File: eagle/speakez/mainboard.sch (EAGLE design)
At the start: 29 parts, among them U1 +12v

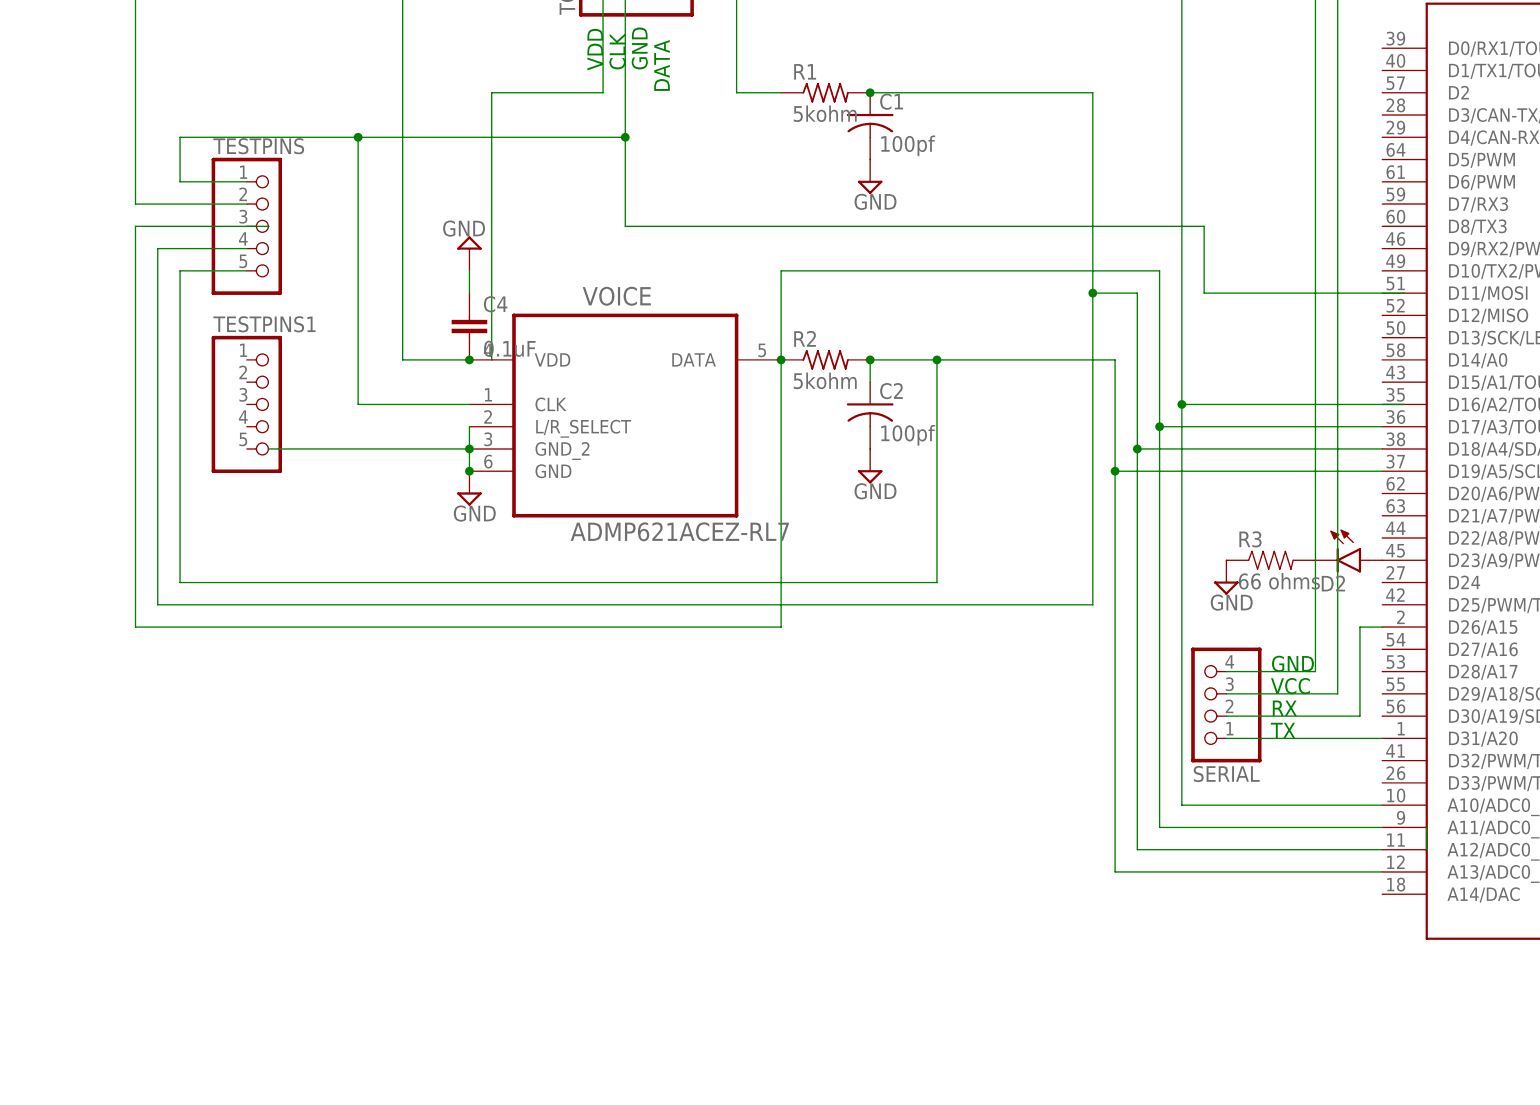
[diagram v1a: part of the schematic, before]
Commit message: added DAC cap + resistor
didn't choose cap value yet. Sent output to a header test pin
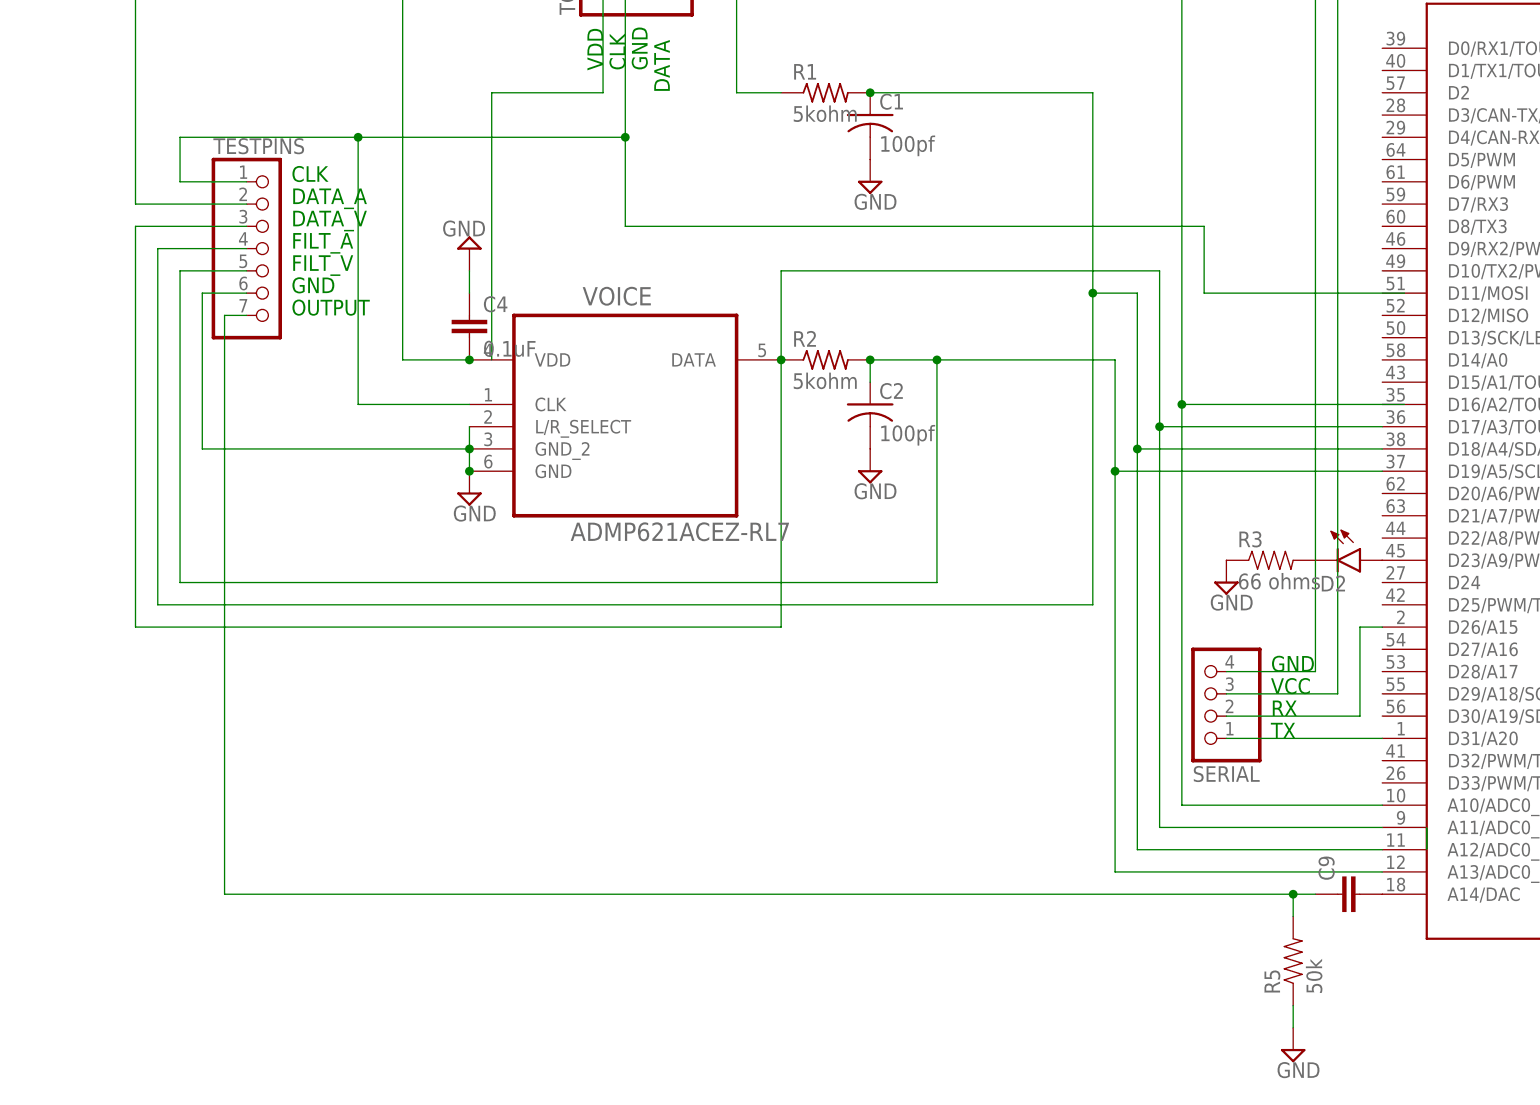
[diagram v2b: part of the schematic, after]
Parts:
- removed TESTPINS1: (no value), pinhead:PINHD-1X5M
- added C9: (no value), SparkFun-Capacitors:CAP0805
- added R5: 50k, SparkFun-Passives:RESISTOR0805-RES
- TESTPINS: device pinhead:PINHD-1X5M -> pinhead:PINHD-1X7
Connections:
- new net N$27: C9.2, U$1.A14/DAC
- new net N$28: C9.1, R5.2, TESTPINS.7
- net GND: now also R5.1, TESTPINS.6
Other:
- note added: "DATA_A"
- note added: "DATA_V"
- note added: "FILT_A"
- note added: "FILT_V"
- note added: "OUTPUT"
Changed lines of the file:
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@@
 <part name="AMBIENT" library="InvenSense-INMP621ACEZ-R7" deviceset="ADMP621ACEZ-RL7" device=""/>
 <part name="VOICE" library="InvenSense-INMP621ACEZ-R7" deviceset="ADMP621ACEZ-RL7" device=""/>
-<part name="TESTPINS" library="pinhead" deviceset="PINHD-1X5" device="M"/>
+<part name="TESTPINS" library="pinhead" deviceset="PINHD-1X7" device=""/>
 <part name="SUPPLY8" library="supply2" deviceset="GND" device=""/>
 <part name="SUPPLY10" library="supply2" deviceset="GND" device=""/>
@@
 <part name="D1" library="SparkFun-DiscreteSemi" deviceset="DIODE" device="SOD123" value="1N5819HW-7-F"/>
 <part name="C3" library="SparkFun-Capacitors" deviceset="CAP" device="0805" value="0.1uF"/>
-<part name="TESTPINS1" library="pinhead" deviceset="PINHD-1X5" device="M"/>
 <part name="SUPPLY4" library="supply2" deviceset="GND" device=""/>
 <part name="U$1" library="Teensy_DIY_v1.0" deviceset="MK20DX256VLH7" device=""/>
@@
 <part name="PROGRAMMER" library="pel_hdr" deviceset="PH1X5" device="-05"/>
 <part name="SERIAL" library="pinhead" deviceset="PINHD-1X4" device=""/>
+<part name="R5" library="SparkFun-Passives" deviceset="RESISTOR" device="0805-RES" value="50k"/>
+<part name="C9" library="SparkFun-Capacitors" deviceset="CAP" device="0805"/>
+<part name="SUPPLY5" library="supply2" deviceset="GND" device=""/>
 </parts>
 <sheets>
@@
 <text x="104.14" y="-12.7" size="1.778" layer="91">TX</text>
 <text x="104.14" y="-10.16" size="1.778" layer="91">RX</text>
+<text x="-7.62" y="50.8" size="1.778" layer="91">CLK</text>
+<text x="-7.62" y="48.26" size="1.778" layer="91">DATA_A</text>
+<text x="-7.62" y="45.72" size="1.778" layer="91">DATA_V</text>
+<text x="-7.62" y="43.18" size="1.778" layer="91">FILT_A</text>
+<text x="-7.62" y="40.64" size="1.778" layer="91">FILT_V</text>
+<text x="-7.62" y="38.1" size="1.778" layer="91">GND</text>
+<text x="-7.62" y="35.56" size="1.778" layer="91">OUTPUT</text>
 </plain>
 <instances>
@@
 <instance part="AMBIENT" gate="A" x="-68.58" y="45.72"/>
 <instance part="VOICE" gate="A" x="30.48" y="27.94"/>
-<instance part="TESTPINS" gate="A" x="-10.16" y="45.72"/>
+<instance part="TESTPINS" gate="A" x="-10.16" y="43.18"/>
 <instance part="SUPPLY8" gate="GND" x="12.7" y="15.24"/>
 <instance part="SUPPLY10" gate="GND" x="12.7" y="43.18" rot="R180"/>
@@
 <instance part="D1" gate="G$1" x="121.92" y="104.14" rot="R270"/>
 <instance part="C3" gate="G$1" x="-93.98" y="43.18"/>
-<instance part="TESTPINS1" gate="A" x="-10.16" y="25.4"/>
 <instance part="SUPPLY4" gate="GND" x="33.02" y="88.9" rot="R180"/>
 <instance part="U$1" gate="G$1" x="144.78" y="15.24"/>
@@
 <instance part="PROGRAMMER" gate="G$1" x="198.12" y="-7.62" rot="R180"/>
 <instance part="SERIAL" gate="A" x="96.52" y="-7.62" rot="R180"/>
+<instance part="R5" gate="G$1" x="106.68" y="-38.1" rot="R90"/>
+<instance part="C9" gate="G$1" x="114.3" y="-30.48" rot="R90"/>
+<instance part="SUPPLY5" gate="GND" x="106.68" y="-48.26"/>
 </instances>
 <busses>
@@
 <wire x1="83.82" y1="2.54" x2="-22.86" y2="2.54" width="0.1524" layer="91"/>
 <wire x1="-22.86" y1="2.54" x2="-22.86" y2="43.18" width="0.1524" layer="91"/>
-<pinref part="TESTPINS" gate="A" pin="4"/>
-<wire x1="-12.7" y1="43.18" x2="-22.86" y2="43.18" width="0.1524" layer="91"/>
 <wire x1="83.82" y1="38.1" x2="88.9" y2="38.1" width="0.1524" layer="91"/>
 <junction x="83.82" y="38.1"/>
@@
 <pinref part="U$1" gate="G$1" pin="A12/ADC0_DP3"/>
 <wire x1="88.9" y1="-25.4" x2="116.84" y2="-25.4" width="0.1524" layer="91"/>
+<pinref part="TESTPINS" gate="A" pin="4"/>
+<wire x1="-22.86" y1="43.18" x2="-12.7" y2="43.18" width="0.1524" layer="91"/>
 </segment>
 </net>
@@
 <wire x1="-20.32" y1="40.64" x2="-20.32" y2="5.08" width="0.1524" layer="91"/>
 <wire x1="-20.32" y1="5.08" x2="66.04" y2="5.08" width="0.1524" layer="91"/>
-<pinref part="TESTPINS" gate="A" pin="5"/>
-<wire x1="-12.7" y1="40.64" x2="-20.32" y2="40.64" width="0.1524" layer="91"/>
 <wire x1="86.36" y1="17.78" x2="86.36" y2="30.48" width="0.1524" layer="91"/>
 <wire x1="86.36" y1="30.48" x2="66.04" y2="30.48" width="0.1524" layer="91"/>
@@
 <pinref part="U$1" gate="G$1" pin="A13/ADC0_DM3"/>
 <wire x1="86.36" y1="-27.94" x2="116.84" y2="-27.94" width="0.1524" layer="91"/>
+<pinref part="TESTPINS" gate="A" pin="5"/>
+<wire x1="-20.32" y1="40.64" x2="-12.7" y2="40.64" width="0.1524" layer="91"/>
 </segment>
 </net>
@@
 <junction x="12.7" y="20.32"/>
 <junction x="12.7" y="17.78"/>
-<wire x1="-10.16" y1="20.32" x2="12.7" y2="20.32" width="0.1524" layer="91"/>
+<wire x1="-17.78" y1="20.32" x2="12.7" y2="20.32" width="0.1524" layer="91"/>
+<pinref part="TESTPINS" gate="A" pin="6"/>
+<wire x1="-12.7" y1="38.1" x2="-17.78" y2="38.1" width="0.1524" layer="91"/>
+<wire x1="-17.78" y1="38.1" x2="-17.78" y2="20.32" width="0.1524" layer="91"/>
 </segment>
 <segment>
@@
 <pinref part="R3" gate="G$1" pin="1"/>
 <pinref part="SUPPLY3" gate="GND" pin="GND"/>
+</segment>
+<segment>
+<pinref part="R5" gate="G$1" pin="1"/>
+<pinref part="SUPPLY5" gate="GND" pin="GND"/>
+<wire x1="106.68" y1="-43.18" x2="106.68" y2="-45.72" width="0.1524" layer="91"/>
 </segment>
 </net>
@@
 <wire x1="48.26" y1="0" x2="-25.4" y2="0" width="0.1524" layer="91"/>
 <wire x1="-25.4" y1="0" x2="-25.4" y2="45.72" width="0.1524" layer="91"/>
-<pinref part="TESTPINS" gate="A" pin="3"/>
-<wire x1="-25.4" y1="45.72" x2="-12.7" y2="45.72" width="0.1524" layer="91"/>
-<wire x1="-12.7" y1="45.72" x2="-10.16" y2="45.72" width="0.1524" layer="91"/>
 <wire x1="91.44" y1="22.86" x2="91.44" y2="40.64" width="0.1524" layer="91"/>
 <wire x1="91.44" y1="40.64" x2="48.26" y2="40.64" width="0.1524" layer="91"/>
@@
 <pinref part="U$1" gate="G$1" pin="A11/ADC0_DP0"/>
 <wire x1="91.44" y1="-22.86" x2="116.84" y2="-22.86" width="0.1524" layer="91"/>
+<pinref part="TESTPINS" gate="A" pin="3"/>
+<wire x1="-25.4" y1="45.72" x2="-12.7" y2="45.72" width="0.1524" layer="91"/>
 </segment>
 </net>
@@
 <junction x="0" y="55.88"/>
 <wire x1="-20.32" y1="55.88" x2="-20.32" y2="50.8" width="0.1524" layer="91"/>
-<pinref part="TESTPINS" gate="A" pin="1"/>
-<wire x1="-20.32" y1="50.8" x2="-12.7" y2="50.8" width="0.1524" layer="91"/>
 <wire x1="0" y1="55.88" x2="0" y2="25.4" width="0.1524" layer="91"/>
 <pinref part="VOICE" gate="A" pin="CLK"/>
@@
 <wire x1="119.38" y1="38.1" x2="96.52" y2="38.1" width="0.1524" layer="91"/>
 <wire x1="96.52" y1="38.1" x2="96.52" y2="45.72" width="0.1524" layer="91"/>
+<pinref part="TESTPINS" gate="A" pin="1"/>
+<wire x1="-20.32" y1="50.8" x2="-12.7" y2="50.8" width="0.1524" layer="91"/>
 </segment>
 </net>
@@
 <pinref part="TOAMBIENT" gate="A" pin="4"/>
 <wire x1="35.56" y1="73.66" x2="43.18" y2="73.66" width="0.1524" layer="91"/>
-<pinref part="TESTPINS" gate="A" pin="2"/>
 <pinref part="R1" gate="G$1" pin="1"/>
 <wire x1="43.18" y1="60.96" x2="48.26" y2="60.96" width="0.1524" layer="91"/>
@@
 <wire x1="43.18" y1="83.82" x2="-25.4" y2="83.82" width="0.1524" layer="91"/>
 <wire x1="-25.4" y1="83.82" x2="-25.4" y2="48.26" width="0.1524" layer="91"/>
-<wire x1="-25.4" y1="48.26" x2="-12.7" y2="48.26" width="0.1524" layer="91"/>
 <junction x="43.18" y="73.66"/>
 <wire x1="43.18" y1="73.66" x2="93.98" y2="73.66" width="0.1524" layer="91"/>
@@
 <pinref part="U$1" gate="G$1" pin="A10/ADC0_DM0"/>
 <wire x1="93.98" y1="-20.32" x2="116.84" y2="-20.32" width="0.1524" layer="91"/>
+<pinref part="TESTPINS" gate="A" pin="2"/>
+<wire x1="-25.4" y1="48.26" x2="-12.7" y2="48.26" width="0.1524" layer="91"/>
 </segment>
 </net>
@@
 </segment>
 </net>
+<net name="N$27" class="0">
+<segment>
+<pinref part="U$1" gate="G$1" pin="A14/DAC"/>
+<pinref part="C9" gate="G$1" pin="2"/>
+</segment>
+</net>
+<net name="N$28" class="0">
+<segment>
+<pinref part="C9" gate="G$1" pin="1"/>
+<wire x1="109.22" y1="-30.48" x2="106.68" y2="-30.48" width="0.1524" layer="91"/>
+<pinref part="R5" gate="G$1" pin="2"/>
+<wire x1="106.68" y1="-30.48" x2="106.68" y2="-33.02" width="0.1524" layer="91"/>
+<wire x1="106.68" y1="-30.48" x2="-15.24" y2="-30.48" width="0.1524" layer="91"/>
+<junction x="106.68" y="-30.48"/>
+<pinref part="TESTPINS" gate="A" pin="7"/>
+<wire x1="-12.7" y1="35.56" x2="-15.24" y2="35.56" width="0.1524" layer="91"/>
+<wire x1="-15.24" y1="35.56" x2="-15.24" y2="-30.48" width="0.1524" layer="91"/>
+</segment>
+</net>

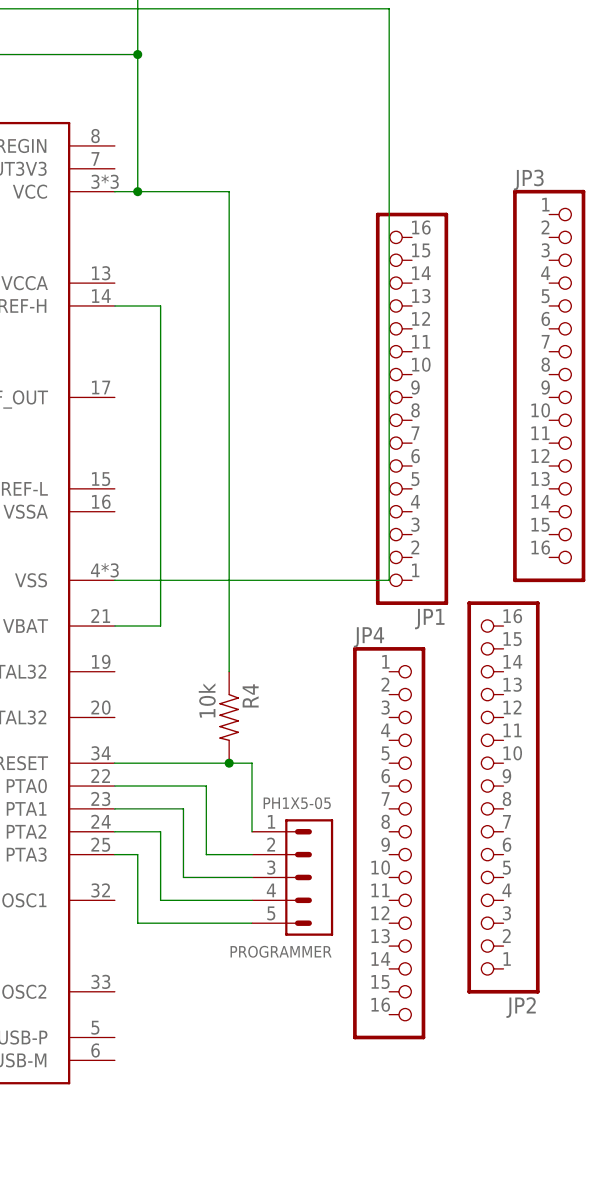
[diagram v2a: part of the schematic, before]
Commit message: test pins for VCC and RESET
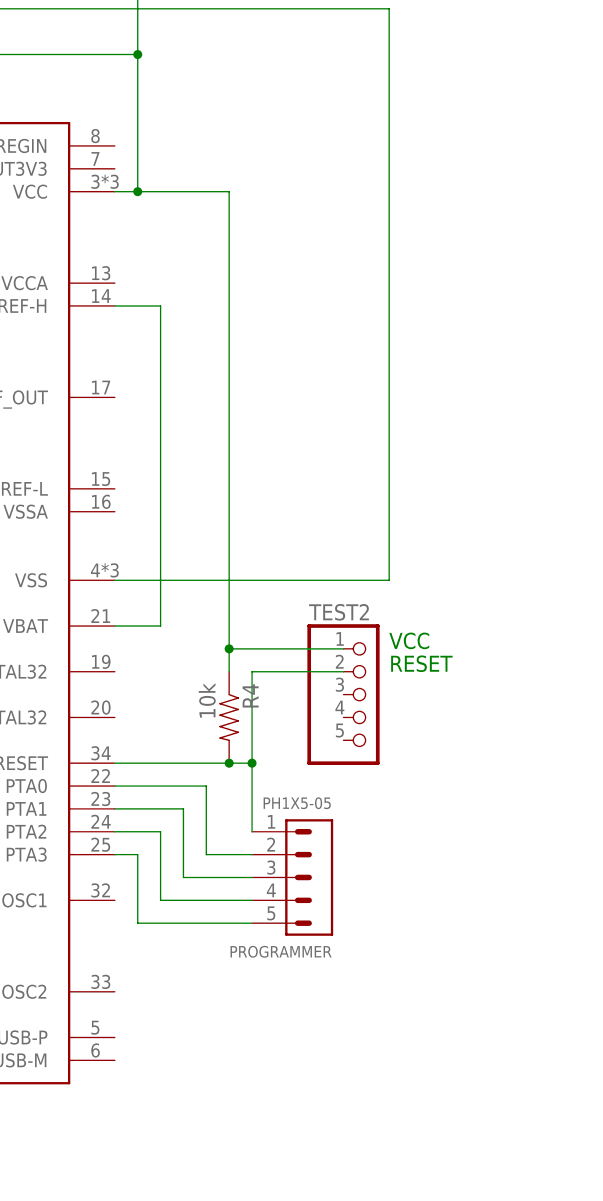
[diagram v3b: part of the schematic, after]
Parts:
- removed JP1, JP2, JP3, JP4: (no value), pinhead:PINHD-1X16
- added TEST2: (no value), pinhead:PINHD-1X5
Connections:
- net N$16: now also TEST2.1
- net N$20: now also TEST2.2
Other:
- note added: "RESET"
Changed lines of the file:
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@@
 <part name="SUPPLY4" library="supply2" deviceset="GND" device=""/>
 <part name="U$1" library="Teensy_DIY_v1.0" deviceset="MK20DX256VLH7" device=""/>
-<part name="JP1" library="pinhead" deviceset="PINHD-1X16" device=""/>
-<part name="JP2" library="pinhead" deviceset="PINHD-1X16" device=""/>
-<part name="JP3" library="pinhead" deviceset="PINHD-1X16" device=""/>
-<part name="JP4" library="pinhead" deviceset="PINHD-1X16" device=""/>
 <part name="U1" library="SparkFun-PowerIC" deviceset="V_REG_78XX" device="7812" value="+12v"/>
 <part name="C5" library="SparkFun-Capacitors" deviceset="CAP" device="0805" value="2.2uF"/>
@@
 <part name="C9" library="SparkFun-Capacitors" deviceset="CAP" device="0805"/>
 <part name="SUPPLY5" library="supply2" deviceset="GND" device=""/>
+<part name="TEST2" library="pinhead" deviceset="PINHD-1X5" device=""/>
 </parts>
 <sheets>
@@
 <text x="-7.62" y="38.1" size="1.778" layer="91">GND</text>
 <text x="-7.62" y="35.56" size="1.778" layer="91">OUTPUT</text>
+<text x="205.74" y="12.7" size="1.778" layer="91">VCC</text>
+<text x="205.74" y="10.16" size="1.778" layer="91">RESET</text>
 </plain>
 <instances>
@@
 <instance part="SUPPLY4" gate="GND" x="33.02" y="88.9" rot="R180"/>
 <instance part="U$1" gate="G$1" x="144.78" y="15.24"/>
-<instance part="JP1" gate="A" x="205.74" y="38.1" rot="R180"/>
-<instance part="JP2" gate="A" x="215.9" y="-5.08" rot="R180"/>
-<instance part="JP3" gate="A" x="226.06" y="43.18"/>
-<instance part="JP4" gate="A" x="208.28" y="-7.62"/>
 <instance part="U1" gate="G$1" x="129.54" y="101.6"/>
 <instance part="C5" gate="G$1" x="121.92" y="86.36"/>
@@
 <instance part="C9" gate="G$1" x="114.3" y="-30.48" rot="R90"/>
 <instance part="SUPPLY5" gate="GND" x="106.68" y="-48.26"/>
+<instance part="TEST2" gate="A" x="203.2" y="7.62"/>
 </instances>
 <busses>
@@
 <junction x="177.8" y="63.5"/>
 <pinref part="R4" gate="G$1" pin="1"/>
-<wire x1="187.96" y1="63.5" x2="187.96" y2="10.16" width="0.1524" layer="91"/>
+<wire x1="187.96" y1="63.5" x2="187.96" y2="12.7" width="0.1524" layer="91"/>
+<wire x1="187.96" y1="12.7" x2="187.96" y2="10.16" width="0.1524" layer="91"/>
 <wire x1="177.8" y1="78.74" x2="111.76" y2="78.74" width="0.1524" layer="91"/>
 <junction x="177.8" y="78.74"/>
@@
 <pinref part="SERIAL" gate="A" pin="3"/>
 <wire x1="111.76" y1="-7.62" x2="99.06" y2="-7.62" width="0.1524" layer="91"/>
+<pinref part="TEST2" gate="A" pin="1"/>
+<wire x1="200.66" y1="12.7" x2="187.96" y2="12.7" width="0.1524" layer="91"/>
+<junction x="187.96" y="12.7"/>
 </segment>
 </net>
@@
 <wire x1="190.5" y1="0" x2="190.5" y2="-7.62" width="0.1524" layer="91"/>
 <junction x="187.96" y="0"/>
-</segment>
-</net>
+<junction x="190.5" y="0"/>
+<pinref part="TEST2" gate="A" pin="2"/>
+<wire x1="190.5" y1="10.16" x2="190.5" y2="0" width="0.1524" layer="91"/>
+<wire x1="200.66" y1="10.16" x2="190.5" y2="10.16" width="0.1524" layer="91"/>
+</segment>
+</net>
